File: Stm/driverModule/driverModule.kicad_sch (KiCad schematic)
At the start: 12 parts, among them U102 ADM7171ACPZ-3.0-R7, U104 TPS5410DR

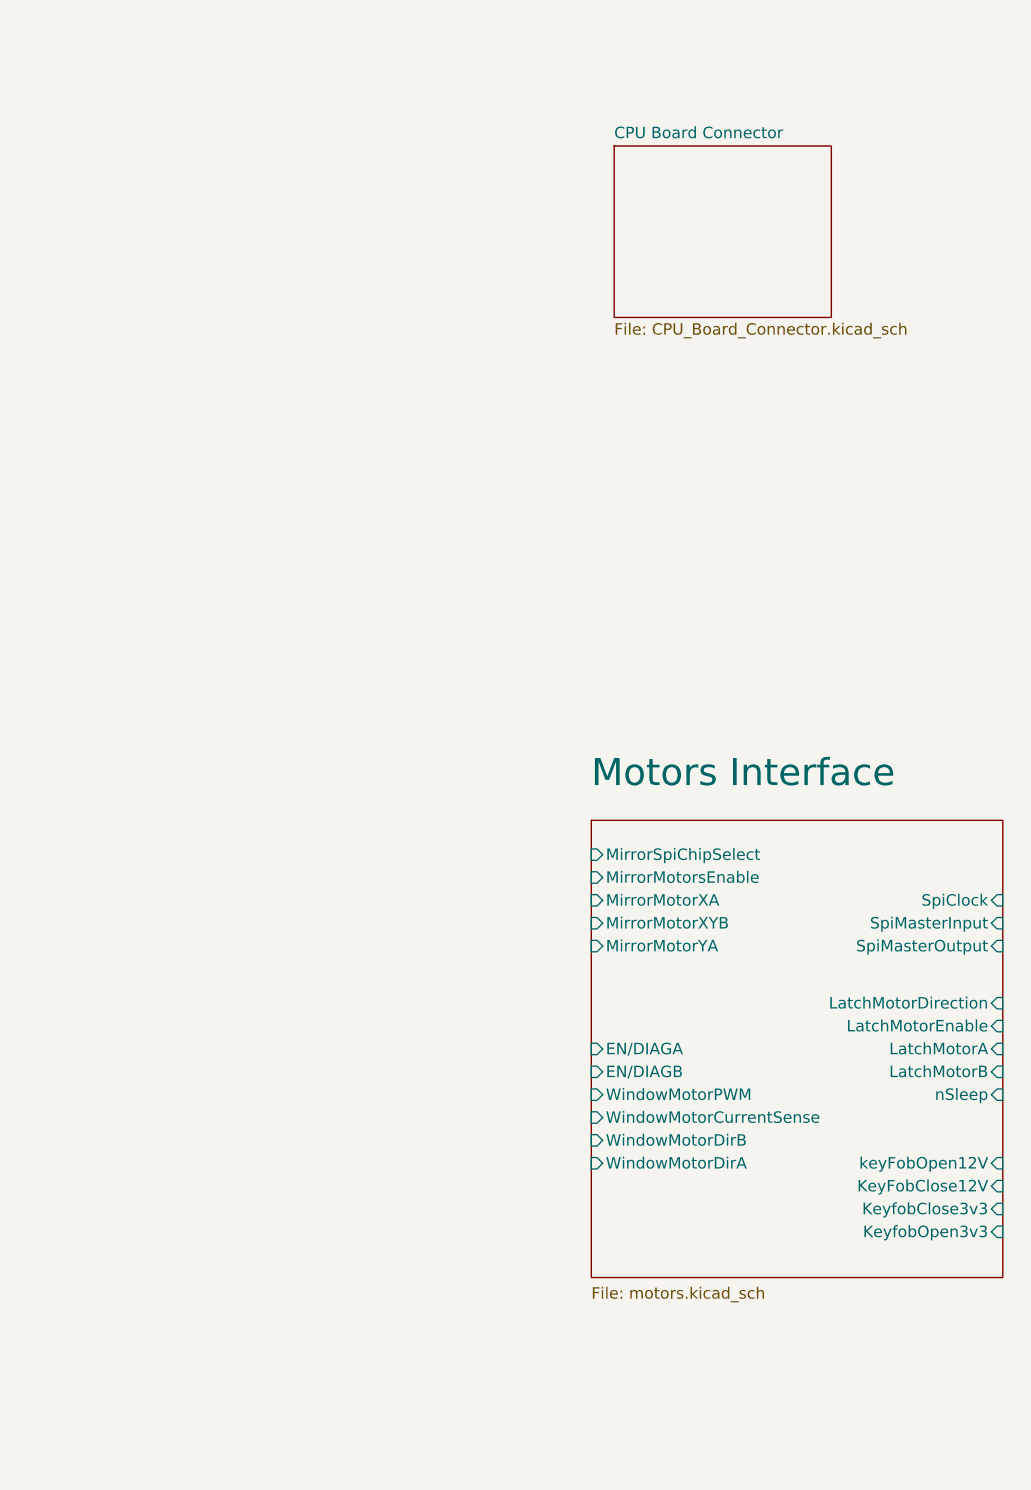
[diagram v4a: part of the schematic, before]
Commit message: Connector
Connect all missing inputs and outputs
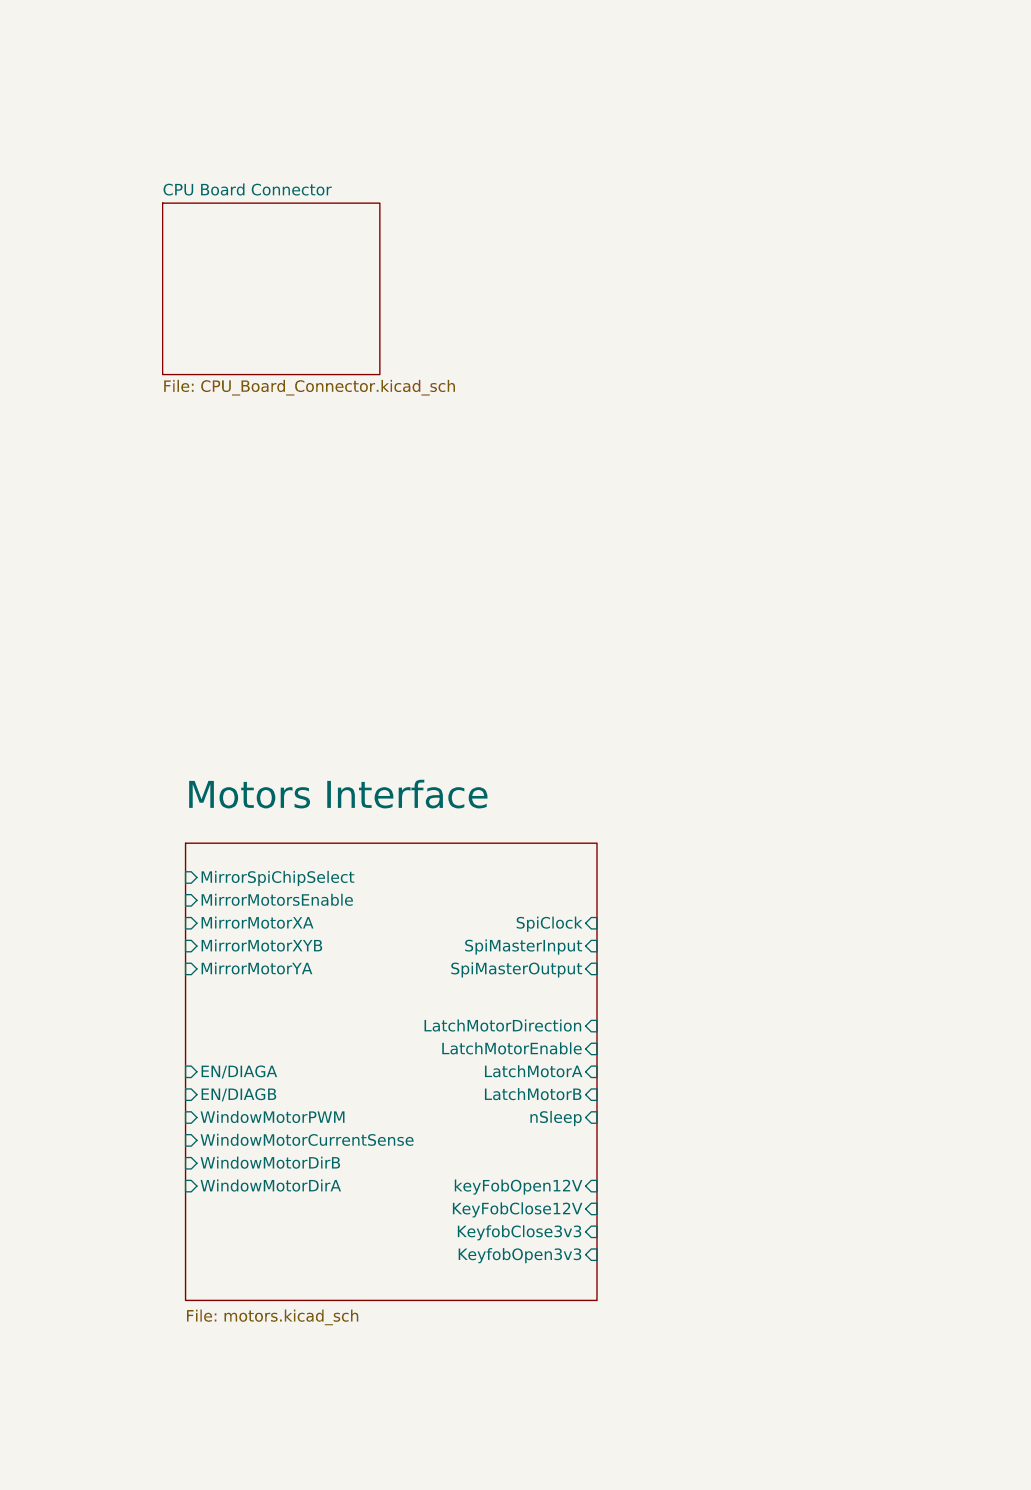
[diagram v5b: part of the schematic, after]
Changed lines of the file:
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@@
 	)
 	(sheet
-		(at 222.25 27.94)
+		(at 172.085 34.29)
 		(size 24.13 19.05)
 		(exclude_from_sim no)
@@
 		)
 		(property "Sheetname" "CPU Board Connector"
-			(at 222.25 27.2284 0)
+			(at 172.085 33.5784 0)
 			(effects
 				(font
@@
 		)
 		(property "Sheetfile" "CPU_Board_Connector.kicad_sch"
-			(at 222.25 47.5746 0)
+			(at 172.085 53.9246 0)
 			(effects
 				(font
@@
 	)
 	(sheet
-		(at 219.71 102.87)
+		(at 174.625 105.41)
 		(size 45.72 50.8)
 		(exclude_from_sim no)
@@
 		)
 		(property "Sheetname" "Motors Interface"
-			(at 219.71 99.314 0)
+			(at 174.625 101.854 0)
 			(effects
 				(font
@@
 		)
 		(property "Sheetfile" "motors.kicad_sch"
-			(at 219.71 154.686 0)
+			(at 174.625 157.226 0)
 			(effects
 				(font
@@
 		)
 		(pin "SpiMasterInput" input
-			(at 265.43 114.3 0)
+			(at 220.345 116.84 0)
 			(effects
 				(font
@@
 		)
 		(pin "LatchMotorB" input
-			(at 265.43 130.81 0)
+			(at 220.345 133.35 0)
 			(effects
 				(font
@@
 		)
 		(pin "MirrorMotorXA" input
-			(at 219.71 111.76 180)
+			(at 174.625 114.3 180)
 			(effects
 				(font
@@
 		)
 		(pin "EN{slash}DIAGA" input
-			(at 219.71 128.27 180)
+			(at 174.625 130.81 180)
 			(effects
 				(font
@@
 		)
 		(pin "WindowMotorCurrentSense" input
-			(at 219.71 135.89 180)
+			(at 174.625 138.43 180)
 			(effects
 				(font
@@
 		)
 		(pin "MirrorMotorXYB" input
-			(at 219.71 114.3 180)
+			(at 174.625 116.84 180)
 			(effects
 				(font
@@
 		)
 		(pin "KeyFobClose12V" input
-			(at 265.43 143.51 0)
+			(at 220.345 146.05 0)
 			(effects
 				(font
@@
 		)
 		(pin "LatchMotorA" input
-			(at 265.43 128.27 0)
+			(at 220.345 130.81 0)
 			(effects
 				(font
@@
 		)
 		(pin "SpiClock" input
-			(at 265.43 111.76 0)
+			(at 220.345 114.3 0)
 			(effects
 				(font
@@
 		)
 		(pin "KeyfobClose3v3" input
-			(at 265.43 146.05 0)
+			(at 220.345 148.59 0)
 			(effects
 				(font
@@
 		)
 		(pin "EN{slash}DIAGB" input
-			(at 219.71 130.81 180)
+			(at 174.625 133.35 180)
 			(effects
 				(font
@@
 		)
 		(pin "WindowMotorDirB" input
-			(at 219.71 138.43 180)
+			(at 174.625 140.97 180)
 			(effects
 				(font
@@
 		)
 		(pin "WindowMotorDirA" input
-			(at 219.71 140.97 180)
+			(at 174.625 143.51 180)
 			(effects
 				(font
@@
 		)
 		(pin "MirrorMotorsEnable" input
-			(at 219.71 109.22 180)
+			(at 174.625 111.76 180)
 			(effects
 				(font
@@
 		)
 		(pin "LatchMotorEnable" input
-			(at 265.43 125.73 0)
+			(at 220.345 128.27 0)
 			(effects
 				(font
@@
 		)
 		(pin "LatchMotorDirection" input
-			(at 265.43 123.19 0)
+			(at 220.345 125.73 0)
 			(effects
 				(font
@@
 		)
 		(pin "WindowMotorPWM" input
-			(at 219.71 133.35 180)
+			(at 174.625 135.89 180)
 			(effects
 				(font
@@
 		)
 		(pin "MirrorSpiChipSelect" input
-			(at 219.71 106.68 180)
+			(at 174.625 109.22 180)
 			(effects
 				(font
@@
 		)
 		(pin "keyFobOpen12V" input
-			(at 265.43 140.97 0)
+			(at 220.345 143.51 0)
 			(effects
 				(font
@@
 		)
 		(pin "KeyfobOpen3v3" input
-			(at 265.43 148.59 0)
+			(at 220.345 151.13 0)
 			(effects
 				(font
@@
 		)
 		(pin "nSleep" input
-			(at 265.43 133.35 0)
+			(at 220.345 135.89 0)
 			(effects
 				(font
@@
 		)
 		(pin "SpiMasterOutput" input
-			(at 265.43 116.84 0)
+			(at 220.345 119.38 0)
 			(effects
 				(font
@@
 		)
 		(pin "MirrorMotorYA" input
-			(at 219.71 116.84 180)
-			(effects
-				(font
+			(at 174.625 119.38 180)
+			(effects
+				(font

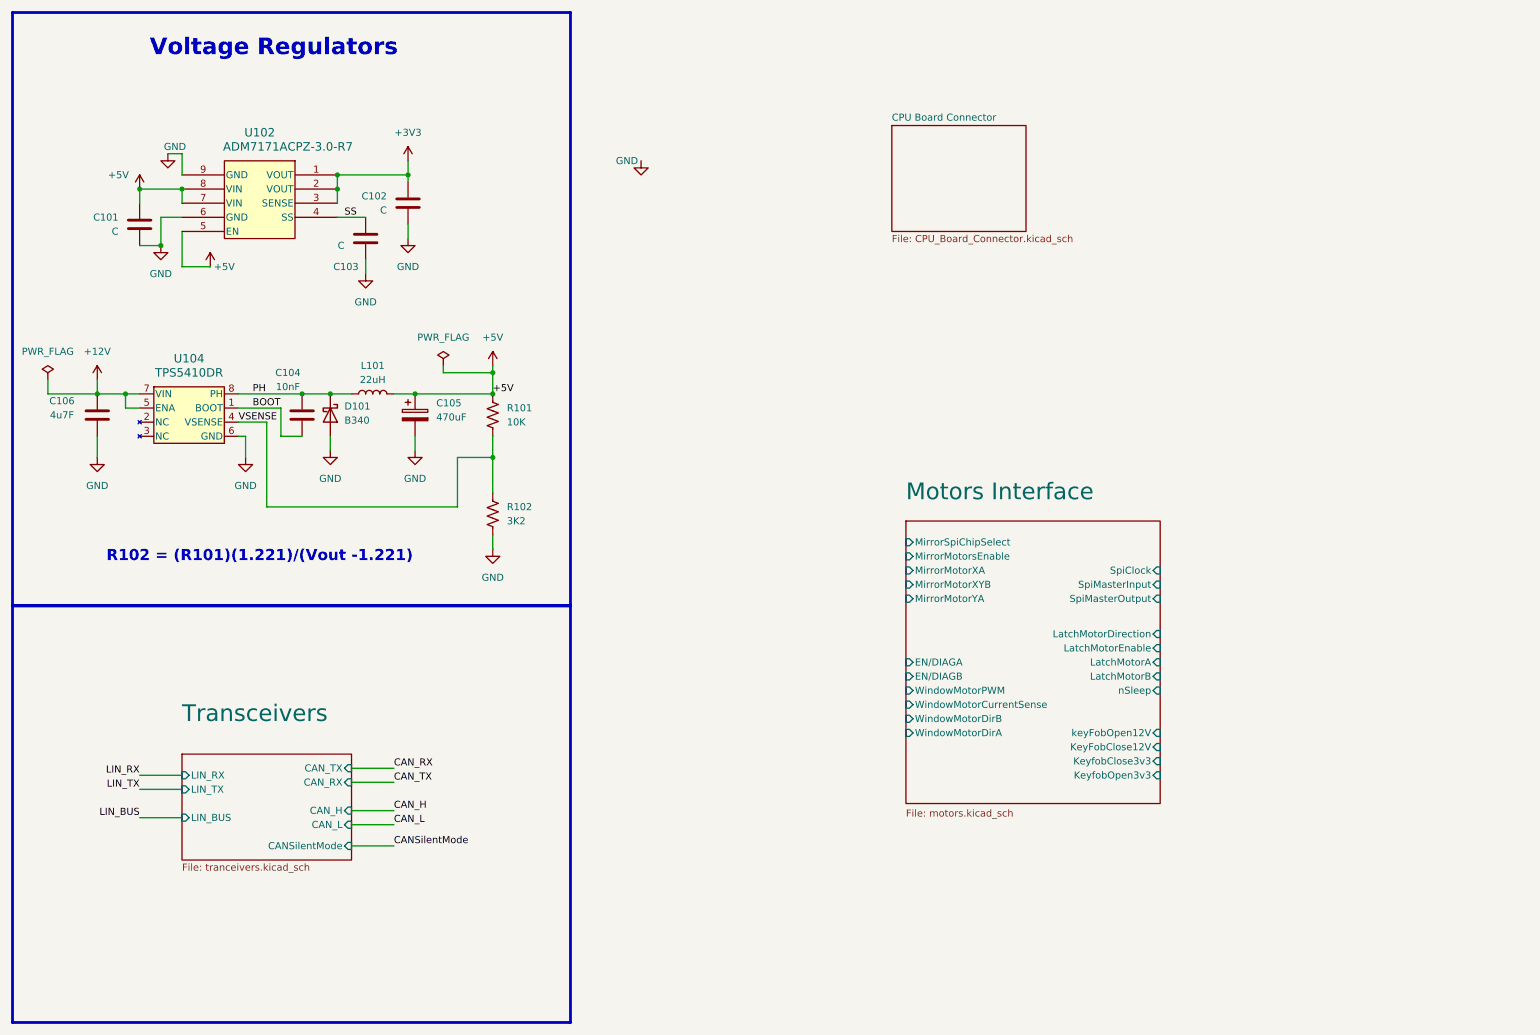
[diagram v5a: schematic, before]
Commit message: Connectors
Remove some enable signals
Added Harness connectors
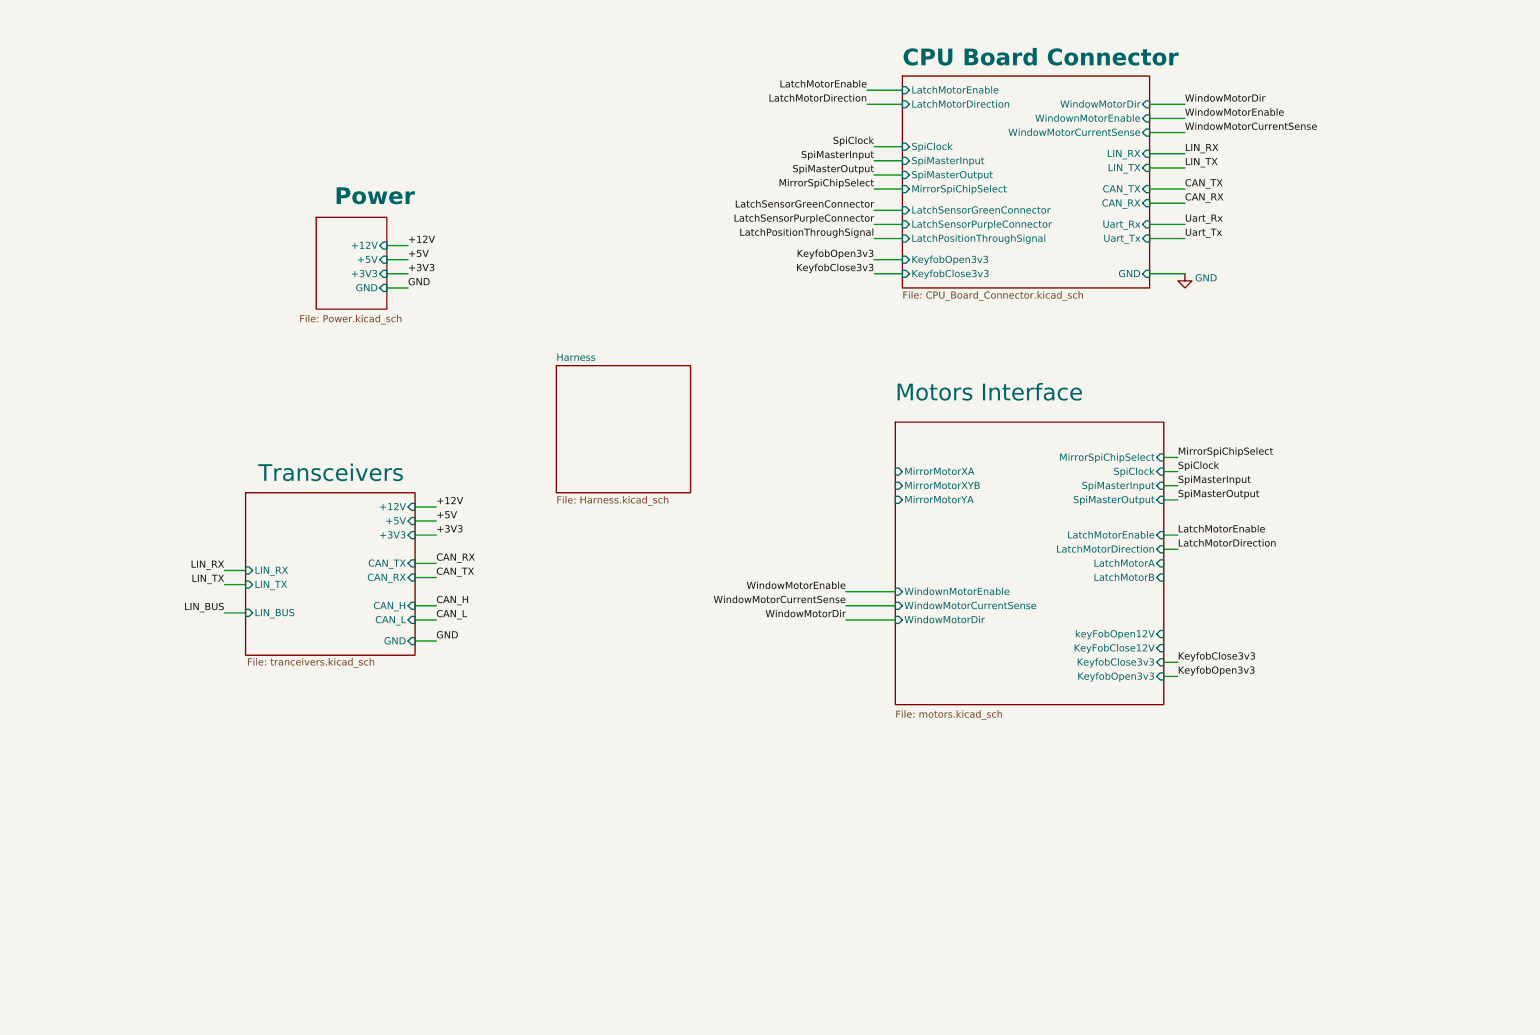
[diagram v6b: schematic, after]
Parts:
- removed C101, C102, C103: C, Capacitor_SMD:C_0402_1005Metric_Pad0.74x0.62mm_HandSolder, symbol Device:C
- removed C104: 10nF, Capacitor_SMD:C_0805_2012Metric, symbol Device:C
- removed C105: 470uF, Capacitor_SMD:CP_Elec_10x10, symbol Device:C_Polarized
- removed C106: 4u7F, Capacitor_SMD:C_0805_2012Metric, symbol Device:C
- removed D101: B340, Diode_SMD:D_SMC, symbol Diode:B340
- removed L101: 22uH, Local_Footprints:L-SMD-13.45x12.6X5.0mm, symbol Device:L
- removed R101: 10K, Resistor_SMD:R_0402_1005Metric_Pad0.72x0.64mm_HandSolder, symbol Device:R_US
- removed R102: 3K2, Resistor_SMD:R_0402_1005Metric_Pad0.72x0.64mm_HandSolder, symbol Device:R_US
- removed U102: ADM7171ACPZ-3.0-R7, Local_Footprints:LFCSP-8-1EP_3x3mm_P0.5mm_EP_1.70x2.54mm, symbol Local_symbols:ADM7171ACPZ-3.0-R7
- removed U104: TPS5410DR, Local_Footprints:SOIC-8-1EP_3.9x4.9mm_P1.27mm, symbol Local_symbols:TPS5410DR
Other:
- added sheet Harness (Harness.kicad_sch)
- added sheet Power (Power.kicad_sch)
- sheet CPU Board Connector ports: added CAN_RX, CAN_TX, GND, KeyfobClose3v3, KeyfobOpen3v3, LIN_RX, LIN_TX, LatchMotorDirection, LatchMotorEnable, LatchPositionThroughSignal, LatchSensorGreenConnector, LatchSensorPurpleConnector, MirrorSpiChipSelect, SpiClock, SpiMasterInput, SpiMasterOutput, Uart_Rx, Uart_Tx, WindowMotorCurrentSense, WindowMotorDir, WindownMotorEnable; removed none
- sheet Motors Interface ports: added WindowMotorDir, WindownMotorEnable; removed EN/DIAGA, EN/DIAGB, MirrorMotorsEnable, WindowMotorDirA, WindowMotorDirB, WindowMotorPWM, nSleep
- sheet Transceivers ports: added +12V, +3V3, +5V, GND; removed CANSilentMode
- note removed: "R102 = (R101)(1.221)/(Vout -1.221)"
- note removed: "Voltage Regulators"

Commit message: Update
Add connection to the harness
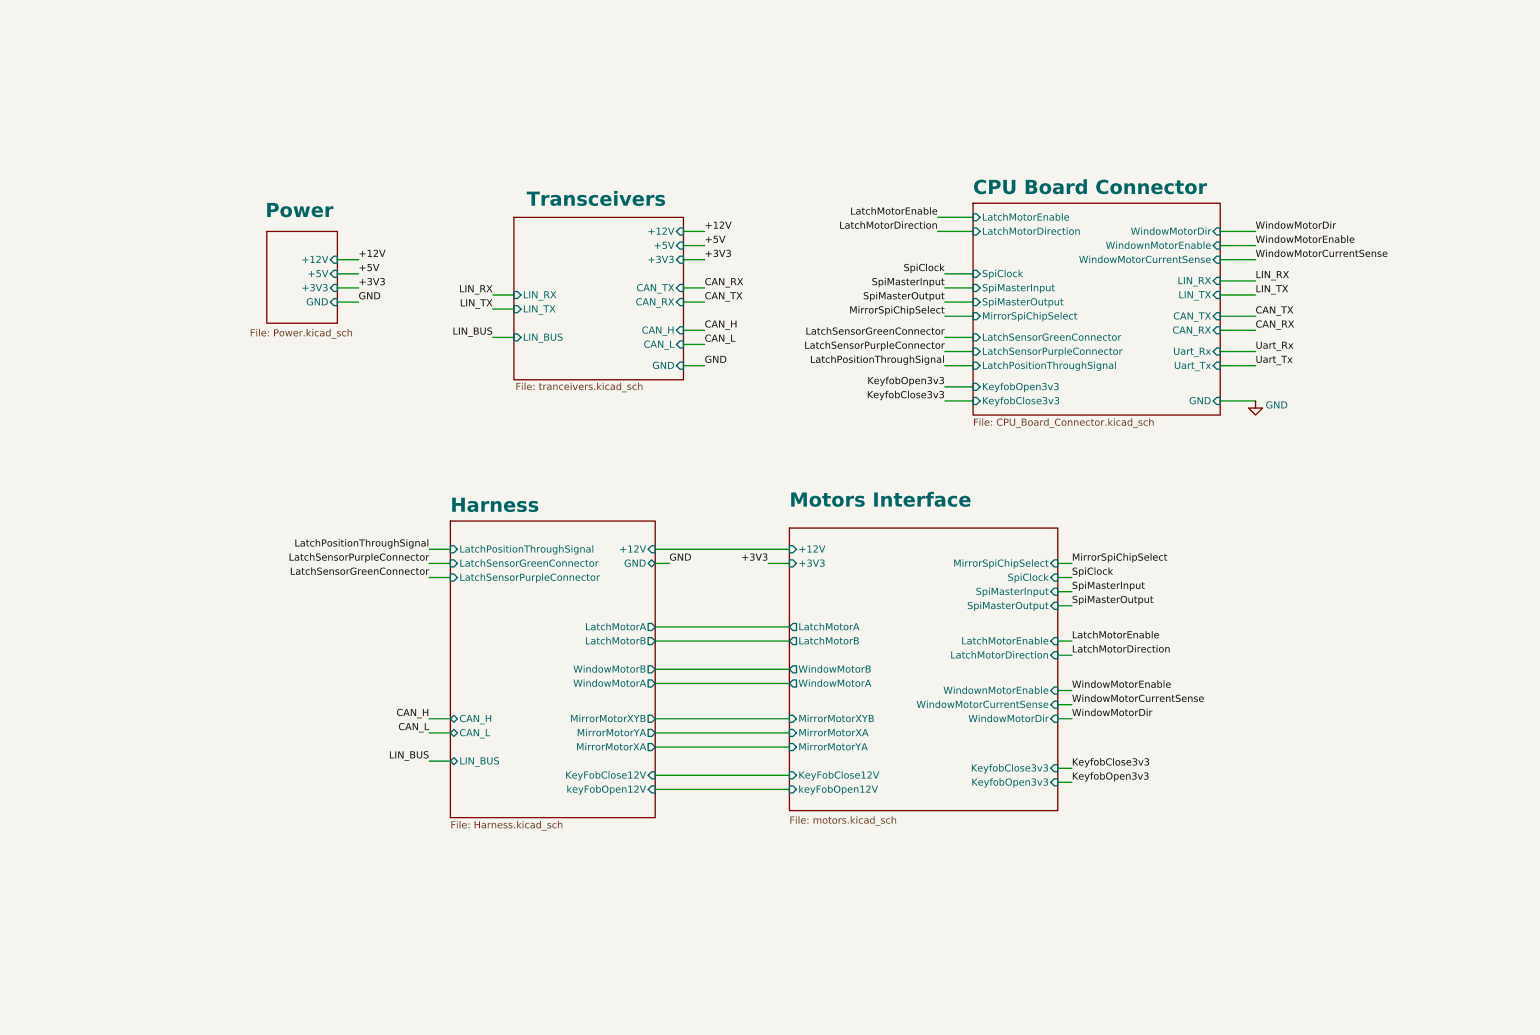
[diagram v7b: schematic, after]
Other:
- sheet Harness ports: added +12V, CAN_H, CAN_L, GND, KeyFobClose12V, LIN_BUS, LatchMotorA, LatchMotorB, LatchPositionThroughSignal, LatchSensorGreenConnector, LatchSensorPurpleConnector, MirrorMotorXA, MirrorMotorXYB, MirrorMotorYA, WindowMotorA, WindowMotorB, keyFobOpen12V; removed none
- sheet Motors Interface ports: added +12V, +3V3, WindowMotorA, WindowMotorB; removed none
